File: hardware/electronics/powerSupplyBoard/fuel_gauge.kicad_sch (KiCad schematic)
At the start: 20 parts, among them J11 PREC002SAAN-RC, Q4 BSS84, Q5 2N7002, Q6 2N7002, U6 BQ34Z100-R2

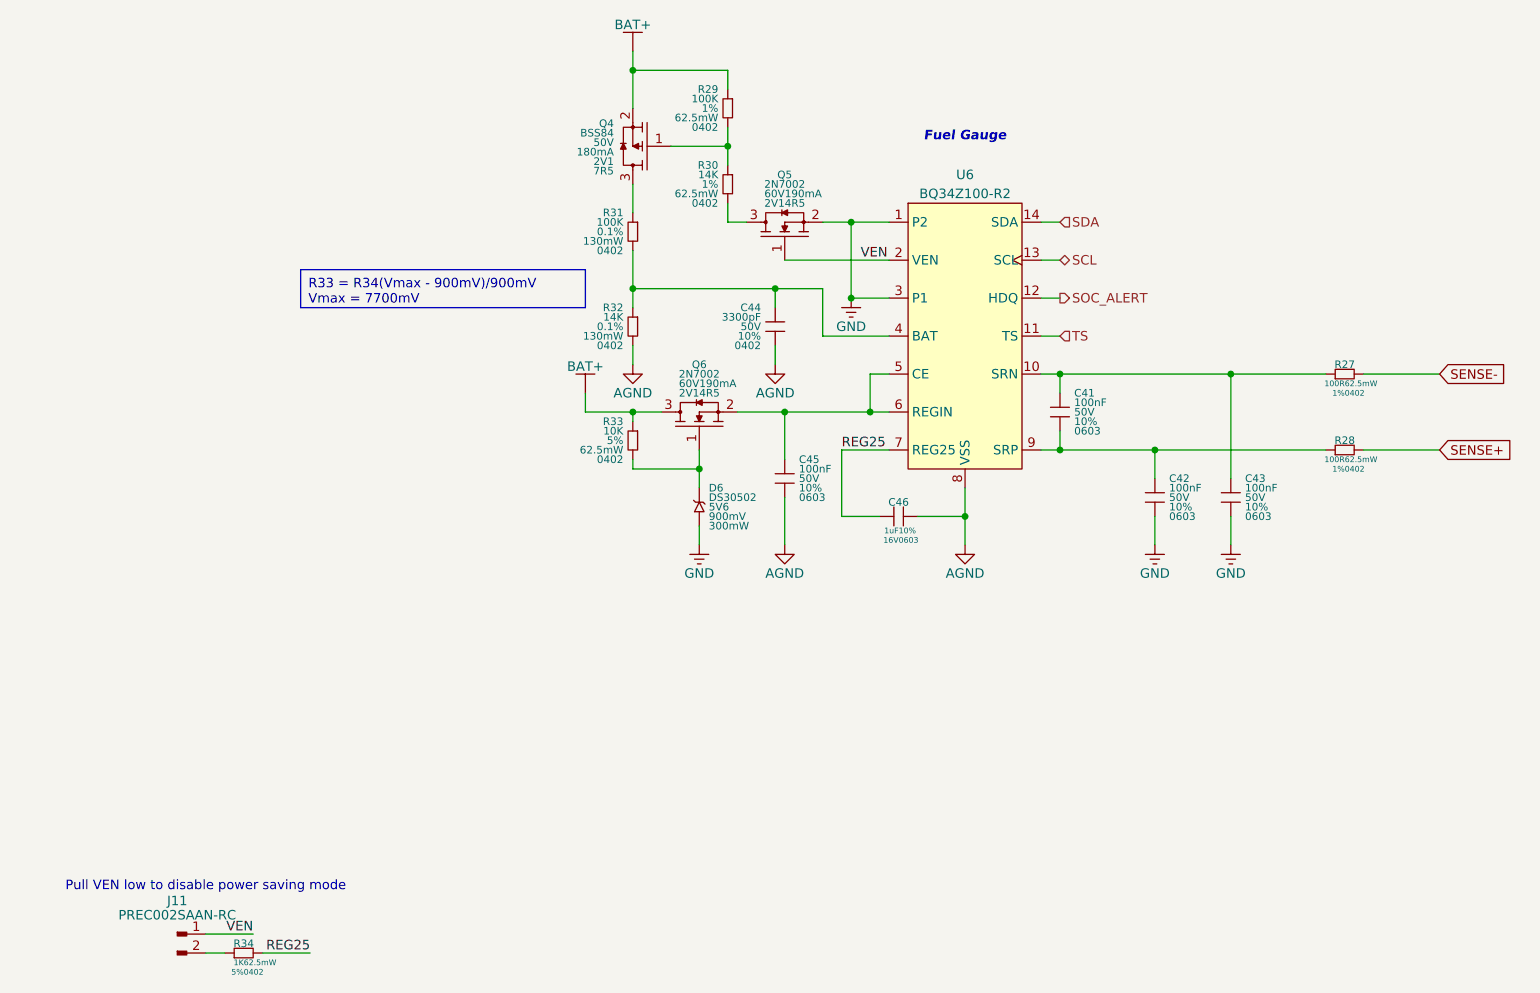
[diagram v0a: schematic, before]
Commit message: removed header pins
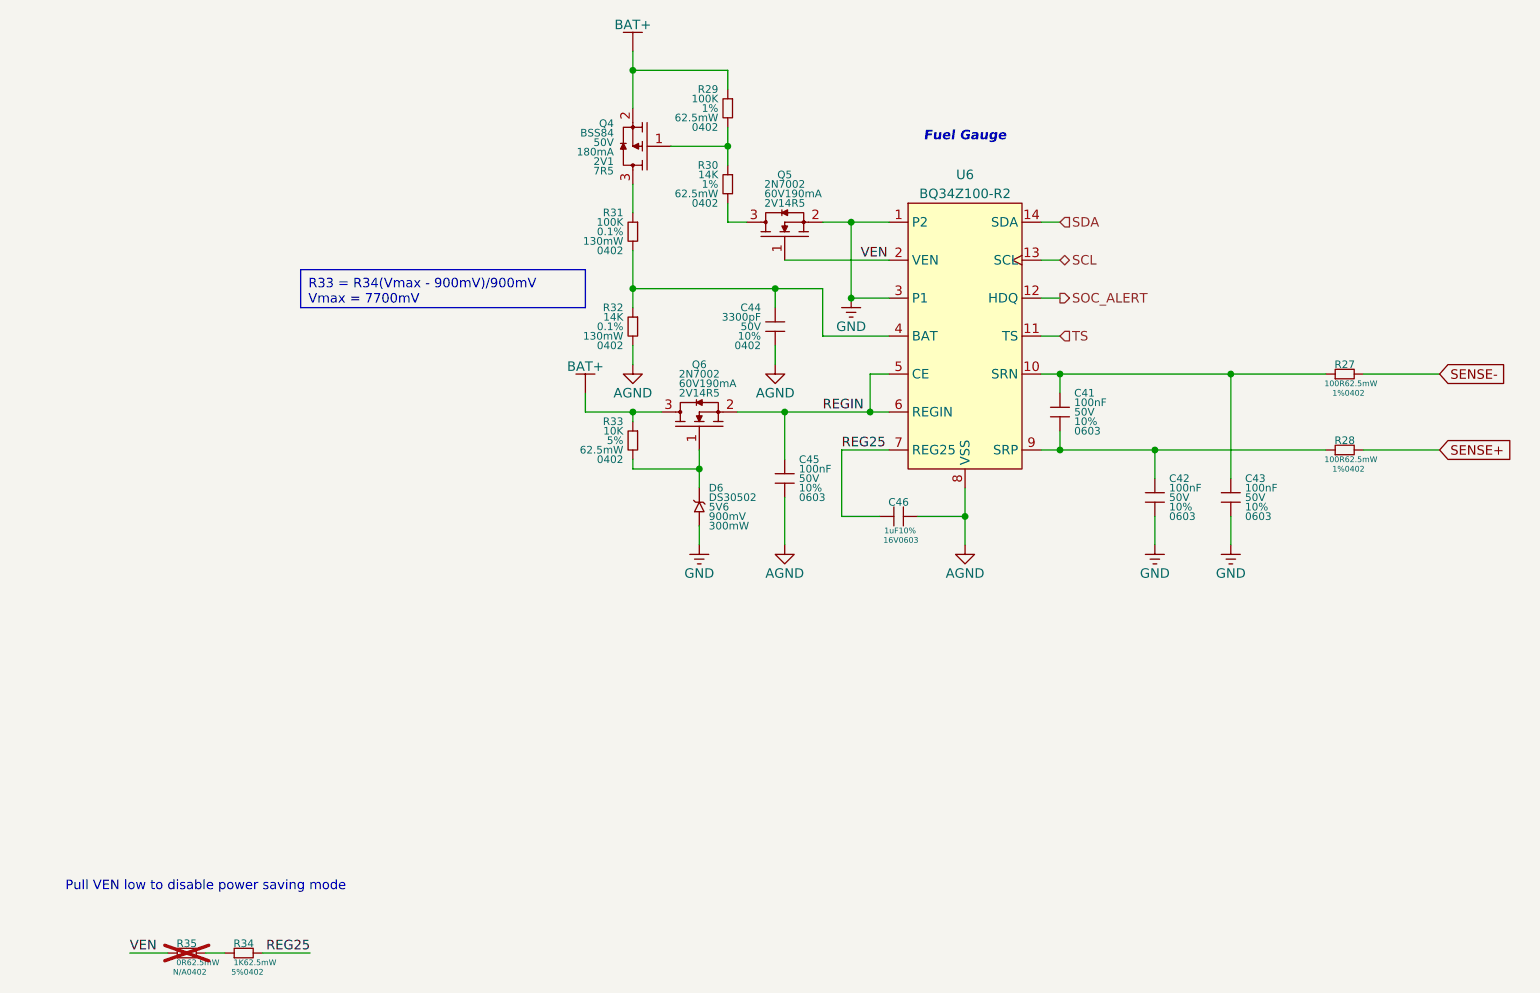
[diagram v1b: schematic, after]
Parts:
- removed J11: PREC002SAAN-RC, lib_fp:conn_01x02_254, symbol lib_sch:Conn_01x02_Pin
- added R35: 0R, lib_fp:CRCW0402, symbol lib_sch:R_horizontal
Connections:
- net VEN: now also R35.1
- net REGIN: now reaches C45.1, Q6.2, U6.5 (CE), U6.6 (REGIN)
- net at R34.1: now also R35.2
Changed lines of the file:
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@@
 	(wire
 		(pts
-			(xy 38.1 187.96) (xy 44.45 187.96)
+			(xy 33.02 190.5) (xy 27.94 190.5)
 		)
 		(stroke
@@
 		)
 	)
-	(label "REG25"
-		(at 52.07 190.5 180)
+	(label "REGIN"
+		(at 120.65 118.11 0)
 		(fields_autoplaced yes)
 		(effects
@@
 				(size 1.27 1.27)
 			)
-			(justify right bottom)
-		)
-	)
-	(label "VEN"
-		(at 125.73 97.79 0)
+			(justify left bottom)
+		)
+	)
+	(label "REG25"
+		(at 52.07 190.5 180)
 		(fields_autoplaced yes)
 		(effects
@@
 				(size 1.27 1.27)
 			)
-			(justify left bottom)
+			(justify right bottom)
 		)
 	)
 	(label "VEN"
-		(at 44.45 187.96 180)
+		(at 125.73 97.79 0)
 		(fields_autoplaced yes)
 		(effects
@@
 				(size 1.27 1.27)
 			)
-			(justify right bottom)
+			(justify left bottom)
+		)
+	)
+	(label "VEN"
+		(at 27.94 190.5 0)
+		(fields_autoplaced yes)
+		(effects
+			(font
+				(size 1.27 1.27)
+			)
+			(justify left bottom)
 		)
 	)
@@
 				(path "/6f3ae1d2-e925-4178-b812-ea14ec542b6c/66c48dda-9393-435e-81e7-77c90d57b98a"
 					(reference "C43")
+					(unit 1)
+				)
+			)
+		)
+	)
+	(symbol
+		(lib_id "lib_sch:R_horizontal")
+		(at 35.56 190.5 0)
+		(unit 1)
+		(exclude_from_sim no)
+		(in_bom yes)
+		(on_board yes)
+		(dnp yes)
+		(fields_autoplaced yes)
+		(property "Reference" "R35"
+			(at 35.56 189.23 0)
+			(do_not_autoplace yes)
+			(effects
+				(font
+					(size 1.016 1.016)
+				)
+			)
+		)
+		(property "Value" "0R"
+			(at 35.56 191.77 0)
+			(do_not_autoplace yes)
+			(effects
+				(font
+					(size 0.762 0.762)
+				)
+				(justify right)
+			)
+		)
+		(property "Footprint" "lib_fp:CRCW0402"
+			(at 33.02 190.5 90)
+			(effects
+				(font
+					(size 1.27 1.27)
+				)
+				(hide yes)
+			)
+		)
+		(property "Datasheet" "datasheets/Vishay-Dale-DRCWe3.pdf"
+			(at 33.02 190.5 90)
+			(effects
+				(font
+					(size 1.27 1.27)
+				)
+				(hide yes)
+			)
+		)
+		(property "Description" "RES SMD 0 OHM JUMPER 1/16W 0402"
+			(at 35.56 190.5 0)
+			(effects
+				(font
+					(size 1.27 1.27)
+				)
+				(hide yes)
+			)
+		)
+		(property "Manufacturer" "Vishay Dale"
+			(at 33.02 190.5 90)
+			(effects
+				(font
+					(size 1.27 1.27)
+				)
+				(hide yes)
+			)
+		)
+		(property "MPN" "CRCW04020000Z0ED"
+			(at 33.02 190.5 90)
+			(effects
+				(font
+					(size 1.27 1.27)
+				)
+				(hide yes)
+			)
+		)
+		(property "DKPN" "541-0.0JCT-ND"
+			(at 35.56 190.5 0)
+			(effects
+				(font
+					(size 1.27 1.27)
+				)
+				(hide yes)
+			)
+		)
+		(property "Tolerance" "N/A"
+			(at 35.56 193.04 0)
+			(do_not_autoplace yes)
+			(effects
+				(font
+					(size 0.762 0.762)
+				)
+				(justify right)
+			)
+		)
+		(property "Power Rating" "62.5mW"
+			(at 35.56 191.77 0)
+			(do_not_autoplace yes)
+			(effects
+				(font
+					(size 0.762 0.762)
+				)
+				(justify left)
+			)
+		)
+		(property "Package" "0402"
+			(at 35.56 193.04 0)
+			(do_not_autoplace yes)
+			(effects
+				(font
+					(size 0.762 0.762)
+				)
+				(justify left)
+			)
+		)
+		(pin "1"
+		)
+		(pin "2"
+		)
+		(instances
+			(project "powerSupplyBoard"
+				(path "/6f3ae1d2-e925-4178-b812-ea14ec542b6c/66c48dda-9393-435e-81e7-77c90d57b98a"
+					(reference "R35")
 					(unit 1)
 				)
@@
 					(unit 1)
 				)
-			)
-		)
-	)
-	(symbol
-		(lib_id "lib_sch:Conn_01x02_Pin")
-		(at 34.29 189.23 0)
-		(unit 1)
-		(exclude_from_sim no)
-		(in_bom yes)
-		(on_board yes)
-		(dnp no)
-		(fields_autoplaced yes)
-		(property "Reference" "J11"
-			(at 34.29 183.515 0)
-			(do_not_autoplace yes)
-			(effects
-				(font
-					(size 1.27 1.27)
-				)
-			)
-		)
-		(property "Value" "PREC002SAAN-RC"
-			(at 34.29 185.42 0)
-			(do_not_autoplace yes)
-			(effects
-				(font
-					(size 1.27 1.27)
-				)
-			)
-		)
-		(property "Footprint" "lib_fp:conn_01x02_254"
-			(at 35.56 190.5 0)
-			(effects
-				(font
-					(size 1.27 1.27)
-				)
-				(hide yes)
-			)
-		)
-		(property "Datasheet" "datasheets/Sullins-Connectors-zRzCzzzSzzN-RC.pdf"
-			(at 35.56 190.5 0)
-			(effects
-				(font
-					(size 1.27 1.27)
-				)
-				(hide yes)
-			)
-		)
-		(property "Description" "CONN HEADER VERT 2POS 2.54MM"
-			(at 35.56 190.5 0)
-			(effects
-				(font
-					(size 1.27 1.27)
-				)
-				(hide yes)
-			)
-		)
-		(property "Manufacturer" "Sullins Connector Solutions"
-			(at 35.56 190.5 0)
-			(effects
-				(font
-					(size 1.27 1.27)
-				)
-				(hide yes)
-			)
-		)
-		(property "MPN" "PREC002SAAN-RC"
-			(at 35.56 190.5 0)
-			(effects
-				(font
-					(size 1.27 1.27)
-				)
-				(hide yes)
-			)
-		)
-		(property "DKPN" "S1012EC-02-ND"
-			(at 35.56 190.5 0)
-			(effects
-				(font
-					(size 1.27 1.27)
-				)
-				(hide yes)
-			)
-		)
-		(pin "2"
-		)
-		(pin "1"
-		)
-		(instances
-			(project "powerSupplyBoard"
-				(path "/6f3ae1d2-e925-4178-b812-ea14ec542b6c/66c48dda-9393-435e-81e7-77c90d57b98a"
-					(reference "J11")
-					(unit 1)
-				)

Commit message: updated part refs
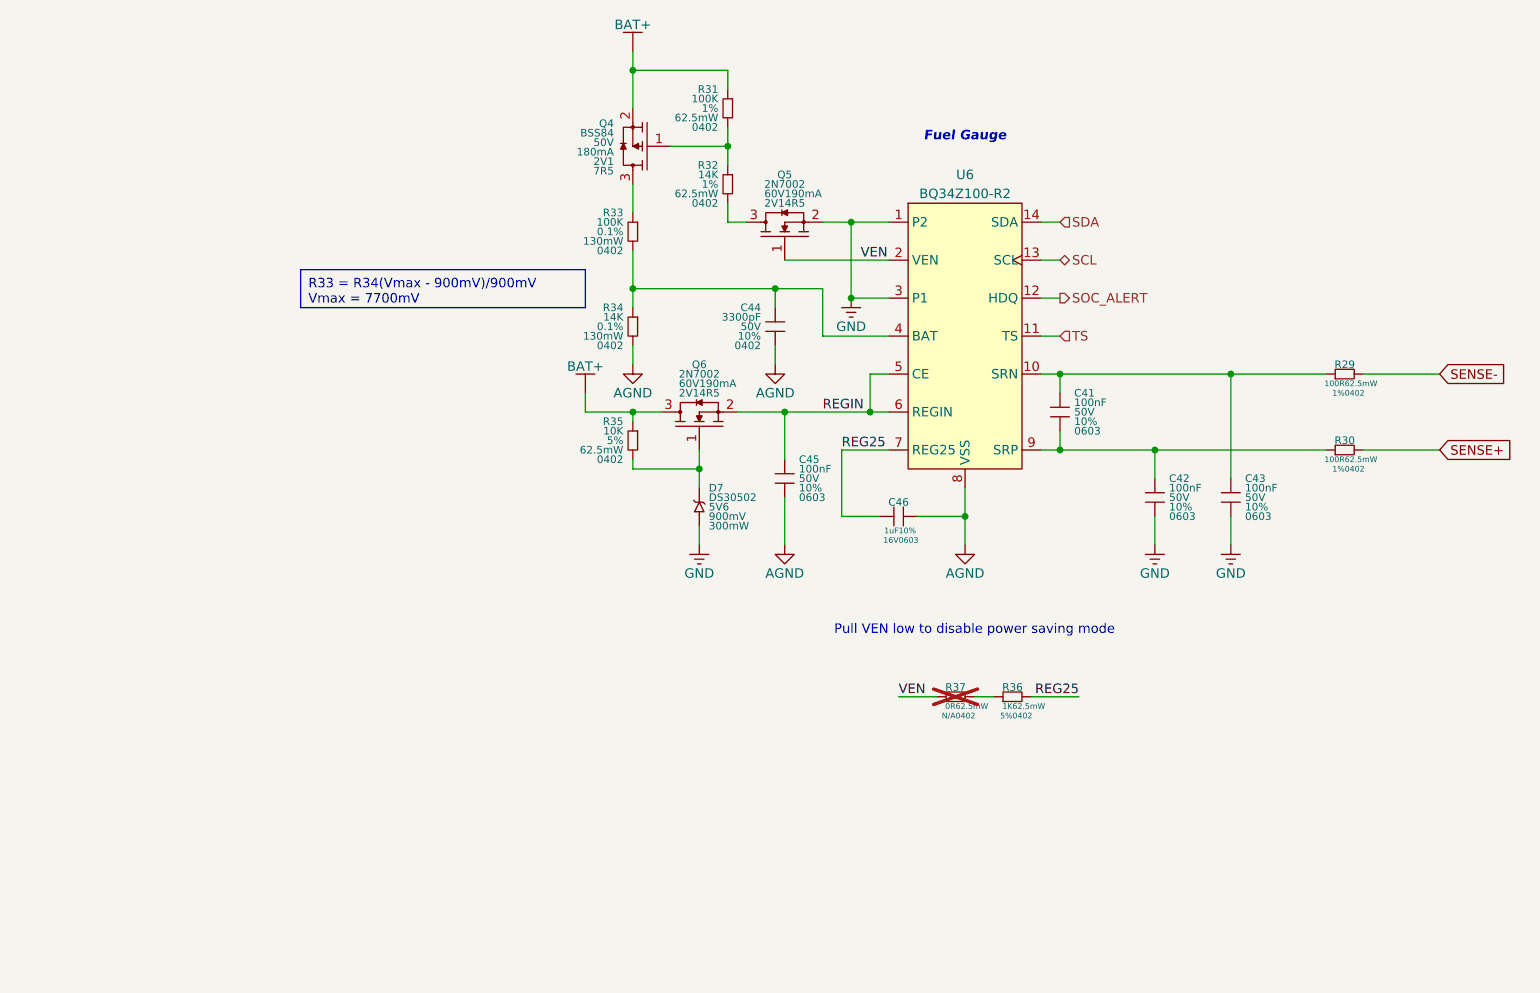
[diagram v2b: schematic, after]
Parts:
- renumbered D6 to D7, R27 to R29, R28 to R30, R29 to R31, R30 to R32, R31 to R33, R32 to R34, R33 to R35, R34 to R36, R35 to R37
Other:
- moved on the sheet: R36, R37
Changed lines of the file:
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@@
 	(title_block
 		(title "LiFePO4 State of Charge")
-		(date "2024-11-03")
+		(date "2024-11-18")
 		(rev "01")
 		(comment 2 "PROTOTYPE")
@@
 	(wire
 		(pts
-			(xy 45.72 190.5) (xy 52.07 190.5)
+			(xy 148.59 156.21) (xy 154.94 156.21)
 		)
 		(stroke
@@
 	(wire
 		(pts
-			(xy 33.02 190.5) (xy 27.94 190.5)
+			(xy 135.89 156.21) (xy 130.81 156.21)
 		)
 		(stroke
@@
 	(wire
 		(pts
-			(xy 38.1 190.5) (xy 40.64 190.5)
+			(xy 140.97 156.21) (xy 143.51 156.21)
 		)
 		(stroke
@@
 	(text "Pull VEN low to disable power saving mode"
 		(exclude_from_sim no)
-		(at 38.1 181.61 0)
+		(at 140.97 147.32 0)
 		(effects
 			(font
@@
 	)
 	(label "REG25"
-		(at 52.07 190.5 180)
+		(at 154.94 156.21 180)
 		(fields_autoplaced yes)
 		(effects
@@
 	)
 	(label "VEN"
-		(at 27.94 190.5 0)
+		(at 130.81 156.21 0)
 		(fields_autoplaced yes)
 		(effects
@@
 		(on_board yes)
 		(dnp no)
-		(property "Reference" "R33"
+		(property "Reference" "R35"
 			(at 93.98 119.38 0)
 			(do_not_autoplace yes)
@@
 			(project "powerSupplyBoard"
 				(path "/6f3ae1d2-e925-4178-b812-ea14ec542b6c/66c48dda-9393-435e-81e7-77c90d57b98a"
-					(reference "R33")
+					(reference "R35")
 					(unit 1)
 				)
@@
 	(symbol
 		(lib_id "lib_sch:R_horizontal")
-		(at 43.18 190.5 0)
+		(at 146.05 156.21 0)
 		(unit 1)
 		(exclude_from_sim no)
@@
 		(dnp no)
 		(fields_autoplaced yes)
-		(property "Reference" "R34"
-			(at 43.18 189.23 0)
+		(property "Reference" "R36"
+			(at 146.05 154.94 0)
 			(do_not_autoplace yes)
 			(effects
@@
 		)
 		(property "Value" "1K"
-			(at 43.18 191.77 0)
+			(at 146.05 157.48 0)
 			(do_not_autoplace yes)
 			(effects
@@
 		)
 		(property "Footprint" "lib_fp:CRCW0402"
-			(at 40.64 190.5 90)
+			(at 143.51 156.21 90)
 			(effects
 				(font
@@
 		)
 		(property "Datasheet" "datasheets/Vishay-Dale-DRCWe3.pdf"
-			(at 40.64 190.5 90)
+			(at 143.51 156.21 90)
 			(effects
 				(font
@@
 		)
 		(property "Description" "RES SMD 1K OHM 5% 1/16W 0402"
-			(at 43.18 190.5 0)
+			(at 146.05 156.21 0)
 			(effects
 				(font
@@
 		)
 		(property "Manufacturer" "Vishay Dale"
-			(at 40.64 190.5 90)
+			(at 143.51 156.21 90)
 			(effects
 				(font
@@
 		)
 		(property "MPN" "CRCW04021K00JNED"
-			(at 40.64 190.5 90)
+			(at 143.51 156.21 90)
 			(effects
 				(font
@@
 		)
 		(property "DKPN" "541-1.0KJCT-ND"
-			(at 43.18 190.5 0)
+			(at 146.05 156.21 0)
 			(effects
 				(font
@@
 		)
 		(property "Tolerance" "5%"
-			(at 43.18 193.04 0)
+			(at 146.05 158.75 0)
 			(do_not_autoplace yes)
 			(effects
@@
 		)
 		(property "Power Rating" "62.5mW"
-			(at 43.18 191.77 0)
+			(at 146.05 157.48 0)
 			(do_not_autoplace yes)
 			(effects
@@
 		)
 		(property "Package" "0402"
-			(at 43.18 193.04 0)
+			(at 146.05 158.75 0)
 			(do_not_autoplace yes)
 			(effects
@@
 			(project "powerSupplyBoard"
 				(path "/6f3ae1d2-e925-4178-b812-ea14ec542b6c/66c48dda-9393-435e-81e7-77c90d57b98a"
-					(reference "R34")
+					(reference "R36")
 					(unit 1)
 				)
@@
 		(dnp no)
 		(fields_autoplaced yes)
-		(property "Reference" "R32"
+		(property "Reference" "R34"
 			(at 93.98 104.14 0)
 			(do_not_autoplace yes)
@@
 			(project "powerSupplyBoard"
 				(path "/6f3ae1d2-e925-4178-b812-ea14ec542b6c/66c48dda-9393-435e-81e7-77c90d57b98a"
-					(reference "R32")
+					(reference "R34")
 					(unit 1)
 				)
@@
 		(on_board yes)
 		(dnp no)
-		(property "Reference" "R29"
+		(property "Reference" "R31"
 			(at 106.68 74.93 0)
 			(do_not_autoplace yes)
@@
 			(project "powerSupplyBoard"
 				(path "/6f3ae1d2-e925-4178-b812-ea14ec542b6c/66c48dda-9393-435e-81e7-77c90d57b98a"
-					(reference "R29")
+					(reference "R31")
 					(unit 1)
 				)
@@
 		(dnp no)
 		(fields_autoplaced yes)
-		(property "Reference" "R28"
+		(property "Reference" "R30"
 			(at 190.5 121.92 0)
 			(do_not_autoplace yes)
@@
 			(project "powerSupplyBoard"
 				(path "/6f3ae1d2-e925-4178-b812-ea14ec542b6c/66c48dda-9393-435e-81e7-77c90d57b98a"
-					(reference "R28")
+					(reference "R30")
 					(unit 1)
 				)
@@
 	(symbol
 		(lib_id "lib_sch:R_horizontal")
-		(at 35.56 190.5 0)
+		(at 138.43 156.21 0)
 		(unit 1)
 		(exclude_from_sim no)
@@
 		(dnp yes)
 		(fields_autoplaced yes)
-		(property "Reference" "R35"
-			(at 35.56 189.23 0)
+		(property "Reference" "R37"
+			(at 138.43 154.94 0)
 			(do_not_autoplace yes)
 			(effects
@@
 		)
 		(property "Value" "0R"
-			(at 35.56 191.77 0)
+			(at 138.43 157.48 0)
 			(do_not_autoplace yes)
 			(effects
@@
 		)
 		(property "Footprint" "lib_fp:CRCW0402"
-			(at 33.02 190.5 90)
+			(at 135.89 156.21 90)
 			(effects
 				(font
@@
 		)
 		(property "Datasheet" "datasheets/Vishay-Dale-DRCWe3.pdf"
-			(at 33.02 190.5 90)
+			(at 135.89 156.21 90)
 			(effects
 				(font
@@
 		)
 		(property "Description" "RES SMD 0 OHM JUMPER 1/16W 0402"
-			(at 35.56 190.5 0)
+			(at 138.43 156.21 0)
 			(effects
 				(font
@@
 		)
 		(property "Manufacturer" "Vishay Dale"
-			(at 33.02 190.5 90)
+			(at 135.89 156.21 90)
 			(effects
 				(font
@@
 		)
 		(property "MPN" "CRCW04020000Z0ED"
-			(at 33.02 190.5 90)
+			(at 135.89 156.21 90)
 			(effects
 				(font
@@
 		)
 		(property "DKPN" "541-0.0JCT-ND"
-			(at 35.56 190.5 0)
+			(at 138.43 156.21 0)
 			(effects
 				(font
@@
 		)
 		(property "Tolerance" "N/A"
-			(at 35.56 193.04 0)
+			(at 138.43 158.75 0)
 			(do_not_autoplace yes)
 			(effects
@@
 		)
 		(property "Power Rating" "62.5mW"
-			(at 35.56 191.77 0)
+			(at 138.43 157.48 0)
 			(do_not_autoplace yes)
 			(effects
@@
 		)
 		(property "Package" "0402"
-			(at 35.56 193.04 0)
+			(at 138.43 158.75 0)
 			(do_not_autoplace yes)
 			(effects
@@
 			(project "powerSupplyBoard"
 				(path "/6f3ae1d2-e925-4178-b812-ea14ec542b6c/66c48dda-9393-435e-81e7-77c90d57b98a"
-					(reference "R35")
+					(reference "R37")
 					(unit 1)
 				)
@@
 		(dnp no)
 		(fields_autoplaced yes)
-		(property "Reference" "D6"
+		(property "Reference" "D7"
 			(at 105.41 128.27 0)
 			(do_not_autoplace yes)
@@
 			(project ""
 				(path "/6f3ae1d2-e925-4178-b812-ea14ec542b6c/66c48dda-9393-435e-81e7-77c90d57b98a"
-					(reference "D6")
+					(reference "D7")
 					(unit 1)
 				)
@@
 		(dnp no)
 		(fields_autoplaced yes)
-		(property "Reference" "R31"
+		(property "Reference" "R33"
 			(at 93.98 91.44 0)
 			(do_not_autoplace yes)
@@
 			(project "powerSupplyBoard"
 				(path "/6f3ae1d2-e925-4178-b812-ea14ec542b6c/66c48dda-9393-435e-81e7-77c90d57b98a"
-					(reference "R31")
+					(reference "R33")
 					(unit 1)
 				)
@@
 		(dnp no)
 		(fields_autoplaced yes)
-		(property "Reference" "R30"
+		(property "Reference" "R32"
 			(at 106.68 85.09 0)
 			(do_not_autoplace yes)
@@
 			(project "powerSupplyBoard"
 				(path "/6f3ae1d2-e925-4178-b812-ea14ec542b6c/66c48dda-9393-435e-81e7-77c90d57b98a"
-					(reference "R30")
+					(reference "R32")
 					(unit 1)
 				)
@@
 		(dnp no)
 		(fields_autoplaced yes)
-		(property "Reference" "R27"
+		(property "Reference" "R29"
 			(at 190.5 111.76 0)
 			(do_not_autoplace yes)
@@
 			(project "powerSupplyBoard"
 				(path "/6f3ae1d2-e925-4178-b812-ea14ec542b6c/66c48dda-9393-435e-81e7-77c90d57b98a"
-					(reference "R27")
+					(reference "R29")
 					(unit 1)
 				)
